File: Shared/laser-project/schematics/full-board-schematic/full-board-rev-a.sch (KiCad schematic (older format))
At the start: 3 parts, among them U1 AT90USB1286

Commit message: Added USB connector and oscillator.
Need to check which package of mcp1825 we have tomorrow; that will
affect the schematic and footprint I put in.
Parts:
- added CON?: USB-MINI-B, symbol USB-MINI-B
- added R? (x2): R, ~, symbol R
- added SW?: SW_PUSH, ~, symbol SW_PUSH
- added X?: CERAMIC-RESONATOR, ~, symbol CERAMIC-RESONATOR
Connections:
- wire segments 5 -> 29
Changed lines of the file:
@@
 LIBS:valves
 LIBS:at90usb1286
-LIBS:full-board-rev-a-cache
+LIBS:ceramic-resonator
+LIBS:mcp1825
 EELAYER 27 0
 EELAYER END
@@
 L GND #PWR?
 U 1 1 526E134D
-P 3550 3400
-F 0 "#PWR?" H 3550 3400 30  0001 C CNN
-F 1 "GND" H 3550 3330 30  0001 C CNN
-F 2 "" H 3550 3400 60  0000 C CNN
-F 3 "" H 3550 3400 60  0000 C CNN
-	1    3550 3400
+P 2000 4400
+F 0 "#PWR?" H 2000 4400 30  0001 C CNN
+F 1 "GND" H 2000 4330 30  0001 C CNN
+F 2 "" H 2000 4400 60  0000 C CNN
+F 3 "" H 2000 4400 60  0000 C CNN
+	1    2000 4400
 	1    0    0    -1
 $EndComp
@@
 L GND #PWR?
 U 1 1 526E135C
-P 3100 2700
-F 0 "#PWR?" H 3100 2700 30  0001 C CNN
-F 1 "GND" H 3100 2630 30  0001 C CNN
-F 2 "" H 3100 2700 60  0000 C CNN
-F 3 "" H 3100 2700 60  0000 C CNN
-	1    3100 2700
+P 2400 2650
+F 0 "#PWR?" H 2400 2650 30  0001 C CNN
+F 1 "GND" H 2400 2580 30  0001 C CNN
+F 2 "" H 2400 2650 60  0000 C CNN
+F 3 "" H 2400 2650 60  0000 C CNN
+	1    2400 2650
 	1    0    0    -1
 $EndComp
@@
 	0    1    1    0
 $EndComp
+$Comp
+L CERAMIC-RESONATOR X?
+U 1 1 526DDAF8
+P 2900 2200
+F 0 "X?" H 3000 2250 60  0000 C CNN
+F 1 "CERAMIC-RESONATOR" H 3000 2050 60  0001 C CNN
+F 2 "~" H 2800 2200 60  0000 C CNN
+F 3 "~" H 2800 2200 60  0000 C CNN
+	1    2900 2200
+	0    -1   -1   0
+$EndComp
+Wire Wire Line
+	2800 2300 3200 2300
+Wire Wire Line
+	2400 1600 2400 2650
+Connection ~ 2400 2300
+$Comp
+L SW_PUSH SW?
+U 1 1 526DDB85
+P 3600 2000
+F 0 "SW?" H 3750 2110 50  0000 C CNN
+F 1 "SW_PUSH" H 3600 1920 50  0000 C CNN
+F 2 "~" H 3600 2000 60  0000 C CNN
+F 3 "~" H 3600 2000 60  0000 C CNN
+	1    3600 2000
+	1    0    0    -1
+$EndComp
+Connection ~ 2950 1900
+Wire Wire Line
+	3300 1600 3300 2000
+Wire Wire Line
+	3900 2000 4100 2000
+Wire Wire Line
+	2400 1600 3300 1600
+Connection ~ 2400 1900
+Wire Wire Line
+	2800 1900 3200 1900
+Wire Wire Line
+	3200 1900 3200 2100
+Wire Wire Line
+	3200 2100 4100 2100
+Wire Wire Line
+	3200 2300 3200 2200
+Wire Wire Line
+	3200 2200 4100 2200
+Connection ~ 2950 2300
+$Comp
+L USB-MINI-B CON?
+U 1 1 526DDD2A
+P 1300 3800
+F 0 "CON?" H 1050 4250 60  0000 C CNN
+F 1 "USB-MINI-B" H 1250 3300 60  0000 C CNN
+F 2 "" H 1300 3800 60  0000 C CNN
+F 3 "" H 1300 3800 60  0000 C CNN
+	1    1300 3800
+	-1   0    0    -1
+$EndComp
+Wire Wire Line
+	1850 4100 2000 4100
+Wire Wire Line
+	2000 4100 2000 4400
+Wire Wire Line
+	1850 3500 1850 1000
+Wire Wire Line
+	1850 1000 4100 1000
+Wire Wire Line
+	4000 1000 4000 1100
+Wire Wire Line
+	4000 1100 4100 1100
+Connection ~ 4000 1000
+$Comp
+L R R?
+U 1 1 526DDE30
+P 2350 3650
+F 0 "R?" V 2430 3650 40  0000 C CNN
+F 1 "R" V 2357 3651 40  0000 C CNN
+F 2 "~" V 2280 3650 30  0000 C CNN
+F 3 "~" H 2350 3650 30  0000 C CNN
+	1    2350 3650
+	0    -1   -1   0
+$EndComp
+$Comp
+L R R?
+U 1 1 526DDE5C
+P 2350 3800
+F 0 "R?" V 2430 3800 40  0000 C CNN
+F 1 "R" V 2357 3801 40  0000 C CNN
+F 2 "~" V 2280 3800 30  0000 C CNN
+F 3 "~" H 2350 3800 30  0000 C CNN
+	1    2350 3800
+	0    -1   -1   0
+$EndComp
+Wire Wire Line
+	1850 3650 2100 3650
+Wire Wire Line
+	2600 3650 2800 3650
+Wire Wire Line
+	2800 3650 2800 2600
+Wire Wire Line
+	2800 2600 4100 2600
+Wire Wire Line
+	1850 3800 2100 3800
+Wire Wire Line
+	2600 3800 2900 3800
+Wire Wire Line
+	2900 3800 2900 2700
+Wire Wire Line
+	2900 2700 4100 2700
 $EndSCHEMATC

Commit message: Added: -Laser Module -Phototransistor -Phase Comparator -Oscillator -supporting circuitry -wiring
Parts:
- added C? (x8): CAP_NP, symbol CAP_NP
- added C?: 0.1u, symbol CAP_NP
- added C?: 0.01u, symbol CAP_NP
- added LD?: LED, symbol LED
- added Q?: OP598C, symbol OP598C
- added R? (x5): R, symbol R
- added U?: DS1077, symbol DS1077
- added U?: AD8302, symbol AD8302
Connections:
- net labels added: AGND, VCC, Vcc
- wire segments 29 -> 128
- no-connect marks 0 -> 1

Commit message: Nearing final version of schematic.
Subunits have been broken out and connected with labels.  and many
parts have been redrawn.  We should no longer be using any standard
library parts except for the ground symbol.

Still need to add the IMU components, their 3.3V regulator, and the
NMOS 5V-3.3V I2C bridge.

After that, we should just need to lock down some component values,
add motor and encoder terminals, and then we should be ready for
layout.
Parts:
- removed C? (x2): CP1, ~, symbol CP1
- removed C? (x8): CAP_NP, symbol CAP_NP
- removed C?: 0.1u, symbol CAP_NP
- removed C?: 0.01u, symbol CAP_NP
- removed CON?: USB-MINI-B, symbol USB-MINI-B
- removed LD?: LED, symbol LED
- removed Q?: OP598C, symbol OP598C
- removed R? (x2): R, ~, symbol R
- removed R? (x5): R, symbol R
- removed SW?: SW_PUSH, ~, symbol SW_PUSH
- removed U?: AD8302, symbol AD8302
- added C1, C2, C3, C4, C5, C6, C7, C8, C9: SMCAP, symbol SMCAP
- added C10, C11, C12, C13: SMCAP, ~, symbol SMCAP
- added CON1, CON2: USB-B, ~, symbol USB-B
- added LD1: OPV332, ~, symbol OPV332
- added R1, R2, R3, R4, R5: SMRES, symbol SMRES
- added R6, R7, R8, R9: SMRES, ~, symbol SMRES
- added SW1: PUSHSWITCH, ~, symbol PUSHSWITCH
- added T1: OP598C, symbol OP598C
- added U3: AD8302, symbol AD8302
- added U4: MCP1825, ~, symbol MCP1825
- X1: renamed from X?; Frequency (none) -> 16MHz
- gave numbers to parts that had none: 1
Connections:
- net labels added: ad8302_inpa, ad8302_inpb, ad8302_mag, ad8302_ofsa, ad8302_ofsb, ad8302_phs, ad8302_vpos, ad8302_vref, mod_sig_1, osc_ctrl0, osc_ctrl1, regulator_5V, regulator_5v, reset_sig, return_sig, twi_scl_5V, twi_sda_5V, usb_5V, usb_d+, usb_d-, xtal1_sig, xtal2_sig
- net labels removed: AGND, VCC, Vcc
- wire segments 128 -> 124

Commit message: Resized the schematic page to US Letter, and made it all fit.
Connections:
- wire segments 124 -> 122
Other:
- moved on the sheet: C1, C10, C11, C12, C13, C2, C3, C4, C5, C6, C7, C8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

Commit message: Fixed some regressions that had happened in the libraries.
I need to be more careful with my commits.

Added a schematic symbol for the bss138, an n-mosfet that will be used
for active conversion between the 5V and 3.3V I2C lines.
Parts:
- removed CON2: USB-B, ~, symbol USB-B
- added C14, C15, C16: SMCAP, ~, symbol SMCAP
- added R10, R11: SMRES, ~, symbol SMRES
- added U5: MCP1825, ~, symbol MCP1825
- R6: Resistance 91k -> 750k
- R7: Resistance 13k -> 68k
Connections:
- net labels added: regulator_3.3V
- wire segments 122 -> 135
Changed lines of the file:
@@
 LIBS:molex-usb-b
 LIBS:push-switch
+LIBS:bss138
 LIBS:full-board-rev-a-cache
 EELAYER 27 0
@@
 Sheet 1 1
 Title "Laser Mapping Project"
-Date "1 nov 2013"
+Date "2 nov 2013"
 Rev "A"
 Comp "Laser Team"
@@
 Wire Wire Line
 	9350 3450 9350 3600
-Wire Wire Line
-	5800 1600 6000 1600
-Wire Wire Line
-	5800 1700 6000 1700
 NoConn ~ 8500 850
 Wire Wire Line
@@
 osc_ctrl1
 Wire Wire Line
-	1150 3950 1150 4050
+	1150 3950 1150 4200
 Wire Wire Line
 	600  4050 1250 4050
@@
 F 2 "~" H 1600 4600 60  0000 C CNN
 F 3 "~" H 1600 4600 60  0000 C CNN
-F 4 "91k" V 1900 4125 60  0000 C CNN "Resistance"
+F 4 "750k" V 1900 4100 60  0000 C CNN "Resistance"
 	1    1850 4300
 	0    -1   -1   0
@@
 F 2 "~" H 1600 4950 60  0000 C CNN
 F 3 "~" H 1600 4950 60  0000 C CNN
-F 4 "13k" V 1900 4475 60  0000 C CNN "Resistance"
+F 4 "68k" V 1900 4475 60  0000 C CNN "Resistance"
 	1    1850 4650
 	0    -1   -1   0
@@
 usb_d+
 $Comp
-L USB-B CON2
-U 1 1 52743649
-P 1750 850
-F 0 "CON2" H 1700 950 60  0000 C CNN
-F 1 "USB-B" H 1750 350 60  0000 C CNN
-F 2 "~" H 1550 1050 60  0000 C CNN
-F 3 "~" H 1550 1050 60  0000 C CNN
-	1    1750 850
-	1    0    0    -1
-$EndComp
-$Comp
-L GND #PWR?
-U 1 1 52743654
-P 2050 1400
-F 0 "#PWR?" H 2050 1400 30  0001 C CNN
-F 1 "GND" H 2050 1330 30  0001 C CNN
-F 2 "" H 2050 1400 60  0000 C CNN
-F 3 "" H 2050 1400 60  0000 C CNN
-	1    2050 1400
-	1    0    0    -1
-$EndComp
-Wire Wire Line
-	1950 1200 2050 1200
-Wire Wire Line
-	2050 1200 2050 1400
-Wire Wire Line
-	1950 900  2450 900
-Text Label 2150 900  0    60   ~ 0
-usb_5V
-$Comp
 L SMCAP C12
 U 1 1 52743812
@@
 Wire Wire Line
 	9350 2600 8900 2600
+$Comp
+L SMCAP C14
+U 1 1 52746D59
+P 1100 4350
+F 0 "C14" V 1250 4450 60  0000 C CNN
+F 1 "SMCAP" H 1350 4400 60  0001 C CNN
+F 2 "~" H 900 4550 60  0000 C CNN
+F 3 "~" H 900 4550 60  0000 C CNN
+F 4 "1u" V 1100 4450 60  0000 C CNN "Capacitance"
+	1    1100 4350
+	0    -1   -1   0
+$EndComp
+Wire Wire Line
+	1150 4350 1150 4500
+Wire Wire Line
+	1150 4500 1350 4500
+Connection ~ 1350 4500
+Wire Wire Line
+	1150 5600 1150 5850
+Wire Wire Line
+	600  5700 1250 5700
+Wire Wire Line
+	1250 5700 1250 5600
+Connection ~ 1150 5700
+Text Label 600  5700 0    60   ~ 0
+usb_5V
+$Comp
+L GND #PWR?
+U 1 1 52746E9E
+P 1350 6450
+F 0 "#PWR?" H 1350 6450 30  0001 C CNN
+F 1 "GND" H 1350 6380 30  0001 C CNN
+F 2 "" H 1350 6450 60  0000 C CNN
+F 3 "" H 1350 6450 60  0000 C CNN
+	1    1350 6450
+	1    0    0    -1
+$EndComp
+Wire Wire Line
+	1350 5600 1350 6450
+Connection ~ 1350 5850
+$Comp
+L MCP1825 U5
+U 1 1 52746EA6
+P 1050 5100
+F 0 "U5" H 1100 5150 60  0000 C CNN
+F 1 "MCP1825" H 1550 5150 60  0000 C CNN
+F 2 "~" H 1050 4900 60  0000 C CNN
+F 3 "~" H 1050 4900 60  0000 C CNN
+	1    1050 5100
+	1    0    0    -1
+$EndComp
+Wire Wire Line
+	1450 5600 1450 5850
+Wire Wire Line
+	1450 5850 1350 5850
+Wire Wire Line
+	1650 5600 1650 6000
+Wire Wire Line
+	1550 5600 1550 5700
+Wire Wire Line
+	1550 5700 2600 5700
+$Comp
+L SMRES R10
+U 1 1 52746EB2
+P 1850 5950
+F 0 "R10" V 2000 5750 60  0000 C CNN
+F 1 "SMRES" H 2150 6000 60  0001 C CNN
+F 2 "~" H 1600 6250 60  0000 C CNN
+F 3 "~" H 1600 6250 60  0000 C CNN
+F 4 "91k" V 1900 5775 60  0000 C CNN "Resistance"
+	1    1850 5950
+	0    -1   -1   0
+$EndComp
+$Comp
+L SMRES R11
+U 1 1 52746EB9
+P 1850 6300
+F 0 "R11" V 2000 6100 60  0000 C CNN
+F 1 "SMRES" H 2150 6350 60  0001 C CNN
+F 2 "~" H 1600 6600 60  0000 C CNN
+F 3 "~" H 1600 6600 60  0000 C CNN
+F 4 "13k" V 1900 6125 60  0000 C CNN "Resistance"
+	1    1850 6300
+	0    -1   -1   0
+$EndComp
+$Comp
+L GND #PWR?
+U 1 1 52746EBF
+P 1900 6450
+F 0 "#PWR?" H 1900 6450 30  0001 C CNN
+F 1 "GND" H 1900 6380 30  0001 C CNN
+F 2 "" H 1900 6450 60  0000 C CNN
+F 3 "" H 1900 6450 60  0000 C CNN
+	1    1900 6450
+	1    0    0    -1
+$EndComp
+Wire Wire Line
+	1900 6300 1900 6450
+Wire Wire Line
+	1900 5950 1900 6050
+Wire Wire Line
+	1650 6000 1900 6000
+Connection ~ 1900 6000
+$Comp
+L SMCAP C16
+U 1 1 52746ECA
+P 2200 5950
+F 0 "C16" V 2300 5750 60  0000 C CNN
+F 1 "SMCAP" H 2450 6000 60  0001 C CNN
+F 2 "~" H 2000 6150 60  0000 C CNN
+F 3 "~" H 2000 6150 60  0000 C CNN
+F 4 "1u" V 2200 5750 60  0000 C CNN "Capacitance"
+	1    2200 5950
+	0    -1   -1   0
+$EndComp
+$Comp
+L GND #PWR?
+U 1 1 52746ED0
+P 2250 6450
+F 0 "#PWR?" H 2250 6450 30  0001 C CNN
+F 1 "GND" H 2250 6380 30  0001 C CNN
+F 2 "" H 2250 6450 60  0000 C CNN
+F 3 "" H 2250 6450 60  0000 C CNN
+	1    2250 6450
+	1    0    0    -1
+$EndComp
+Wire Wire Line
+	2250 5700 2250 5800
+Connection ~ 2250 5700
+Wire Wire Line
+	2250 5950 2250 6450
+Text Label 2250 5700 0    60   ~ 0
+regulator_3.3V
+$Comp
+L SMCAP C15
+U 1 1 52746EDB
+P 1100 6000
+F 0 "C15" V 1250 6100 60  0000 C CNN
+F 1 "SMCAP" H 1350 6050 60  0001 C CNN
+F 2 "~" H 900 6200 60  0000 C CNN
+F 3 "~" H 900 6200 60  0000 C CNN
+F 4 "1u" V 1100 6100 60  0000 C CNN "Capacitance"
+	1    1100 6000
+	0    -1   -1   0
+$EndComp
+Wire Wire Line
+	1150 6000 1150 6150
+Wire Wire Line
+	1150 6150 1350 6150
+Connection ~ 1350 6150
 $EndSCHEMATC

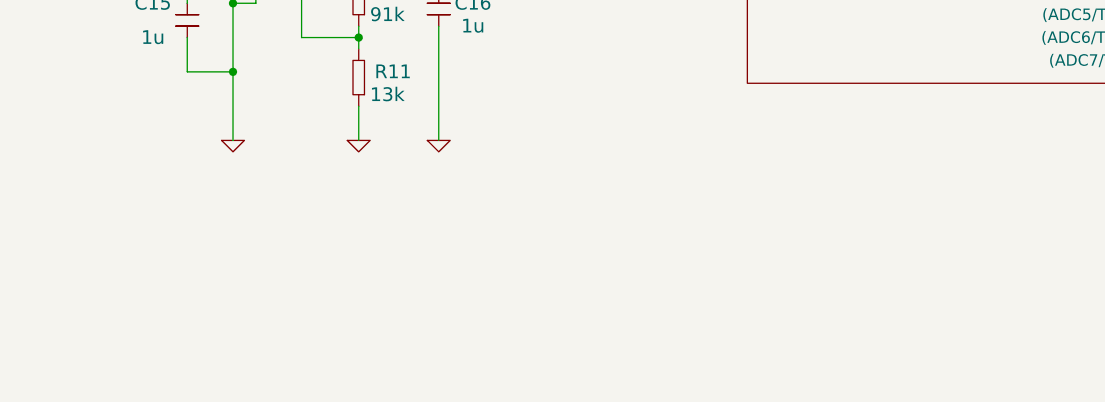
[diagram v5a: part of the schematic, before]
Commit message: Added 5V to 3.3V I2C Converters with BSS138.
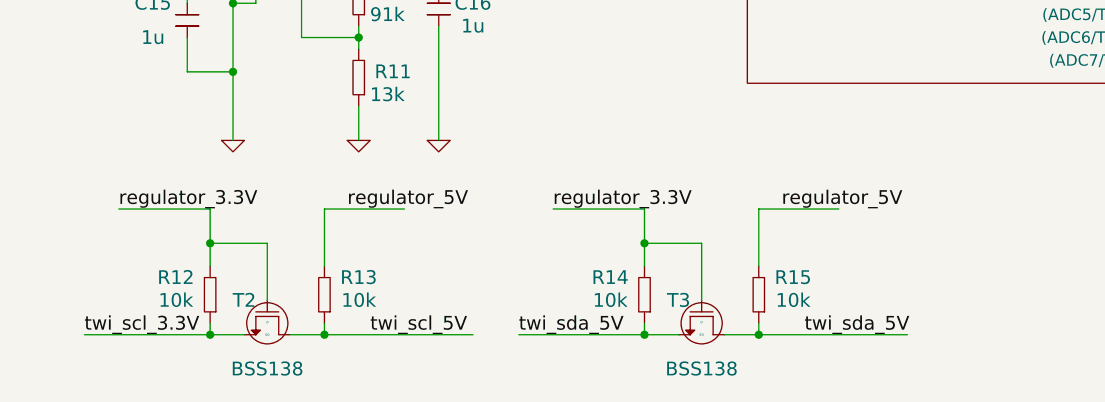
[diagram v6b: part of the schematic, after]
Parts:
- added R12, R13, R14, R15: SMRES, ~, symbol SMRES
- added T2, T3: BSS138, ~, symbol BSS138
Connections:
- net labels added: twi_scl_3.3V
- wire segments 135 -> 155
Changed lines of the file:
@@
 EESchema Schematic File Version 2
 LIBS:power
-LIBS:device
-LIBS:transistors
-LIBS:conn
-LIBS:linear
-LIBS:regul
-LIBS:74xx
-LIBS:cmos4000
-LIBS:adc-dac
-LIBS:memory
-LIBS:xilinx
-LIBS:special
-LIBS:microcontrollers
-LIBS:dsp
-LIBS:microchip
-LIBS:analog_switches
-LIBS:motorola
-LIBS:texas
-LIBS:intel
-LIBS:audio
-LIBS:interface
-LIBS:digital-audio
-LIBS:philips
-LIBS:display
-LIBS:cypress
-LIBS:siliconi
-LIBS:opto
-LIBS:atmel
-LIBS:contrib
-LIBS:valves
 LIBS:at90usb1286
 LIBS:ceramic-resonator
@@
 LIBS:push-switch
 LIBS:bss138
-LIBS:full-board-rev-a-cache
 EELAYER 27 0
 EELAYER END
@@
 	1150 6150 1350 6150
 Connection ~ 1350 6150
+$Comp
+L BSS138 T2
+U 1 1 52747BC6
+P 1600 7150
+F 0 "T2" V 1600 6950 60  0000 C CNN
+F 1 "BSS138" V 1900 7050 60  0000 C CNN
+F 2 "~" H 1400 7350 60  0000 C CNN
+F 3 "~" H 1400 7350 60  0000 C CNN
+	1    1600 7150
+	0    1    1    0
+$EndComp
+$Comp
+L SMRES R13
+U 1 1 52747C02
+P 1700 7250
+F 0 "R13" V 1900 7050 60  0000 C CNN
+F 1 "SMRES" H 2000 7300 60  0001 C CNN
+F 2 "~" H 1450 7550 60  0000 C CNN
+F 3 "~" H 1450 7550 60  0000 C CNN
+F 4 "10k" V 1800 7050 60  0000 C CNN "Resistance"
+	1    1700 7250
+	0    -1   -1   0
+$EndComp
+$Comp
+L SMRES R12
+U 1 1 52747C11
+P 1200 7250
+F 0 "R12" V 1400 7350 60  0000 C CNN
+F 1 "SMRES" H 1500 7300 60  0001 C CNN
+F 2 "~" H 950 7550 60  0000 C CNN
+F 3 "~" H 950 7550 60  0000 C CNN
+F 4 "10k" V 1300 7350 60  0000 C CNN "Resistance"
+	1    1200 7250
+	0    -1   -1   0
+$EndComp
+Wire Wire Line
+	700  7300 1400 7300
+Wire Wire Line
+	1250 7250 1250 7300
+Connection ~ 1250 7300
+Wire Wire Line
+	1600 7300 2400 7300
+Wire Wire Line
+	1750 7250 1750 7300
+Connection ~ 1750 7300
+Wire Wire Line
+	1750 7000 1750 6750
+Wire Wire Line
+	1750 6750 2100 6750
+Wire Wire Line
+	1250 7000 1250 6750
+Wire Wire Line
+	1250 6750 850  6750
+Wire Wire Line
+	1250 6900 1500 6900
+Wire Wire Line
+	1500 6900 1500 7150
+Connection ~ 1250 6900
+Text Label 850  6750 0    60   ~ 0
+regulator_3.3V
+Text Label 1850 6750 0    60   ~ 0
+regulator_5V
+Text Label 1950 7300 0    60   ~ 0
+twi_scl_5V
+Text Label 700  7300 0    60   ~ 0
+twi_scl_3.3V
+$Comp
+L BSS138 T3
+U 1 1 52748162
+P 3500 7150
+F 0 "T3" V 3500 6950 60  0000 C CNN
+F 1 "BSS138" V 3800 7050 60  0000 C CNN
+F 2 "~" H 3300 7350 60  0000 C CNN
+F 3 "~" H 3300 7350 60  0000 C CNN
+	1    3500 7150
+	0    1    1    0
+$EndComp
+$Comp
+L SMRES R15
+U 1 1 52748169
+P 3600 7250
+F 0 "R15" V 3800 7050 60  0000 C CNN
+F 1 "SMRES" H 3900 7300 60  0001 C CNN
+F 2 "~" H 3350 7550 60  0000 C CNN
+F 3 "~" H 3350 7550 60  0000 C CNN
+F 4 "10k" V 3700 7050 60  0000 C CNN "Resistance"
+	1    3600 7250
+	0    -1   -1   0
+$EndComp
+$Comp
+L SMRES R14
+U 1 1 52748170
+P 3100 7250
+F 0 "R14" V 3300 7350 60  0000 C CNN
+F 1 "SMRES" H 3400 7300 60  0001 C CNN
+F 2 "~" H 2850 7550 60  0000 C CNN
+F 3 "~" H 2850 7550 60  0000 C CNN
+F 4 "10k" V 3200 7350 60  0000 C CNN "Resistance"
+	1    3100 7250
+	0    -1   -1   0
+$EndComp
+Wire Wire Line
+	2600 7300 3300 7300
+Wire Wire Line
+	3150 7250 3150 7300
+Connection ~ 3150 7300
+Wire Wire Line
+	3500 7300 4300 7300
+Wire Wire Line
+	3650 7250 3650 7300
+Connection ~ 3650 7300
+Wire Wire Line
+	3650 7000 3650 6750
+Wire Wire Line
+	3650 6750 4000 6750
+Wire Wire Line
+	3150 7000 3150 6750
+Wire Wire Line
+	3150 6750 2750 6750
+Wire Wire Line
+	3150 6900 3400 6900
+Wire Wire Line
+	3400 6900 3400 7150
+Connection ~ 3150 6900
+Text Label 2750 6750 0    60   ~ 0
+regulator_3.3V
+Text Label 3750 6750 0    60   ~ 0
+regulator_5V
+Text Label 3850 7300 0    60   ~ 0
+twi_sda_5V
+Text Label 2600 7300 0    60   ~ 0
+twi_sda_5V
 $EndSCHEMATC

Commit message: Added alternate schematic. Only difference is replacing the microcontroller schematic with a teensy++2.0 block. To be determined which is necessary. Need to create header connections for Teensy and select packages and associated footprints for components. PCB layout soon to follow...
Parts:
- added U?: TEENSYPP2, MODULE, symbol TEENSYPP2
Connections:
- net labels added: A0, A1, A2, A3, A4, A5, A6, A7, B0, B1, B2, B3, B4, B5, B6, B7, C2, C3, C4, C5, C6, C7, D2, D3, D4, D5, D6, D7, E0, E1, E4, E5, E6, E7, F2, F3, F4, F5, F6, F7
- wire segments 155 -> 238
